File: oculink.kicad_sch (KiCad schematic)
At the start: 9 parts, among them J1 OCuLink_x4_Amphenol_G14A42121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

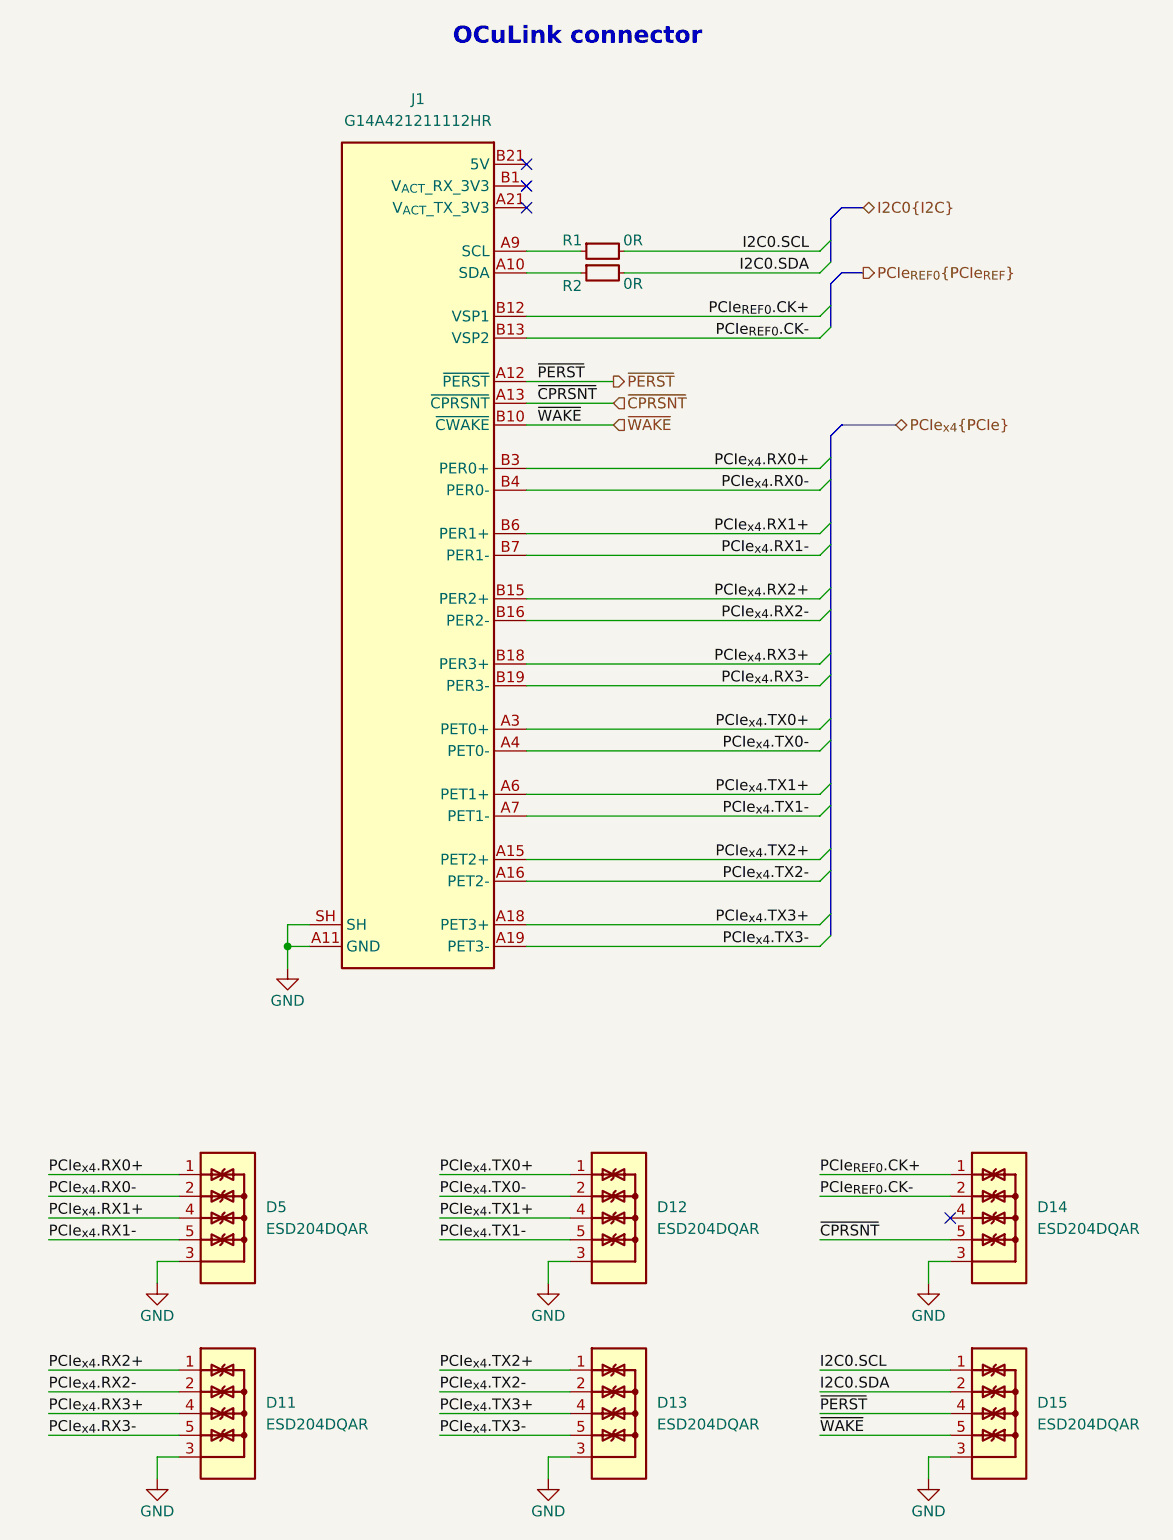
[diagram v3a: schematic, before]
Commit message: [#79426] Add optional clock generator
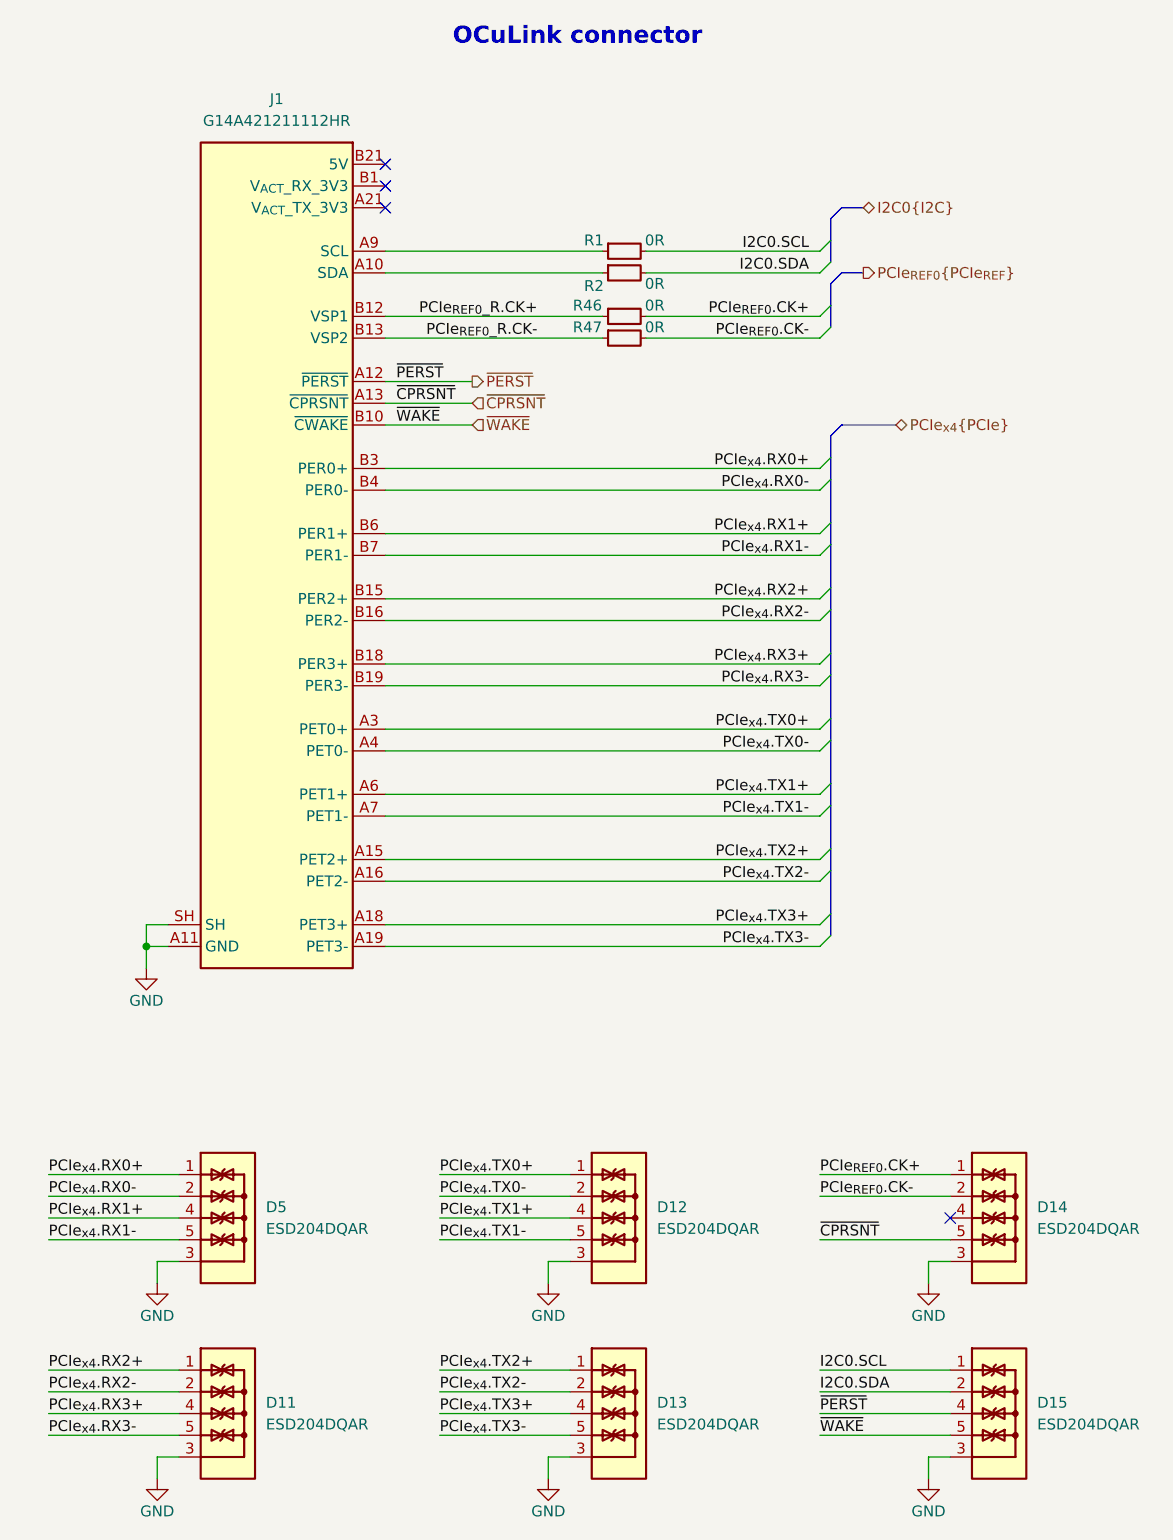
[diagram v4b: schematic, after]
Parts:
- added R46, R47: R_0R_0402, antmicro-footprints:R_0402_1005Metric, symbol antmicroResistors0402:R_0R_0402
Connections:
- net PCIe_{REF0}.CK+: now also R46.2; no longer J1.B12 (VSP1)
- net PCIe_{REF0}.CK-: now also R47.2; no longer J1.B13 (VSP2)
- new net PCIe_{REF0}_R.CK+: J1.B12 (VSP1), R46.1
- new net PCIe_{REF0}_R.CK-: J1.B13 (VSP2), R47.1
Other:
- moved on the sheet: J1, R1, R2

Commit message: [#79426] Add 0R to OCuLink control signals
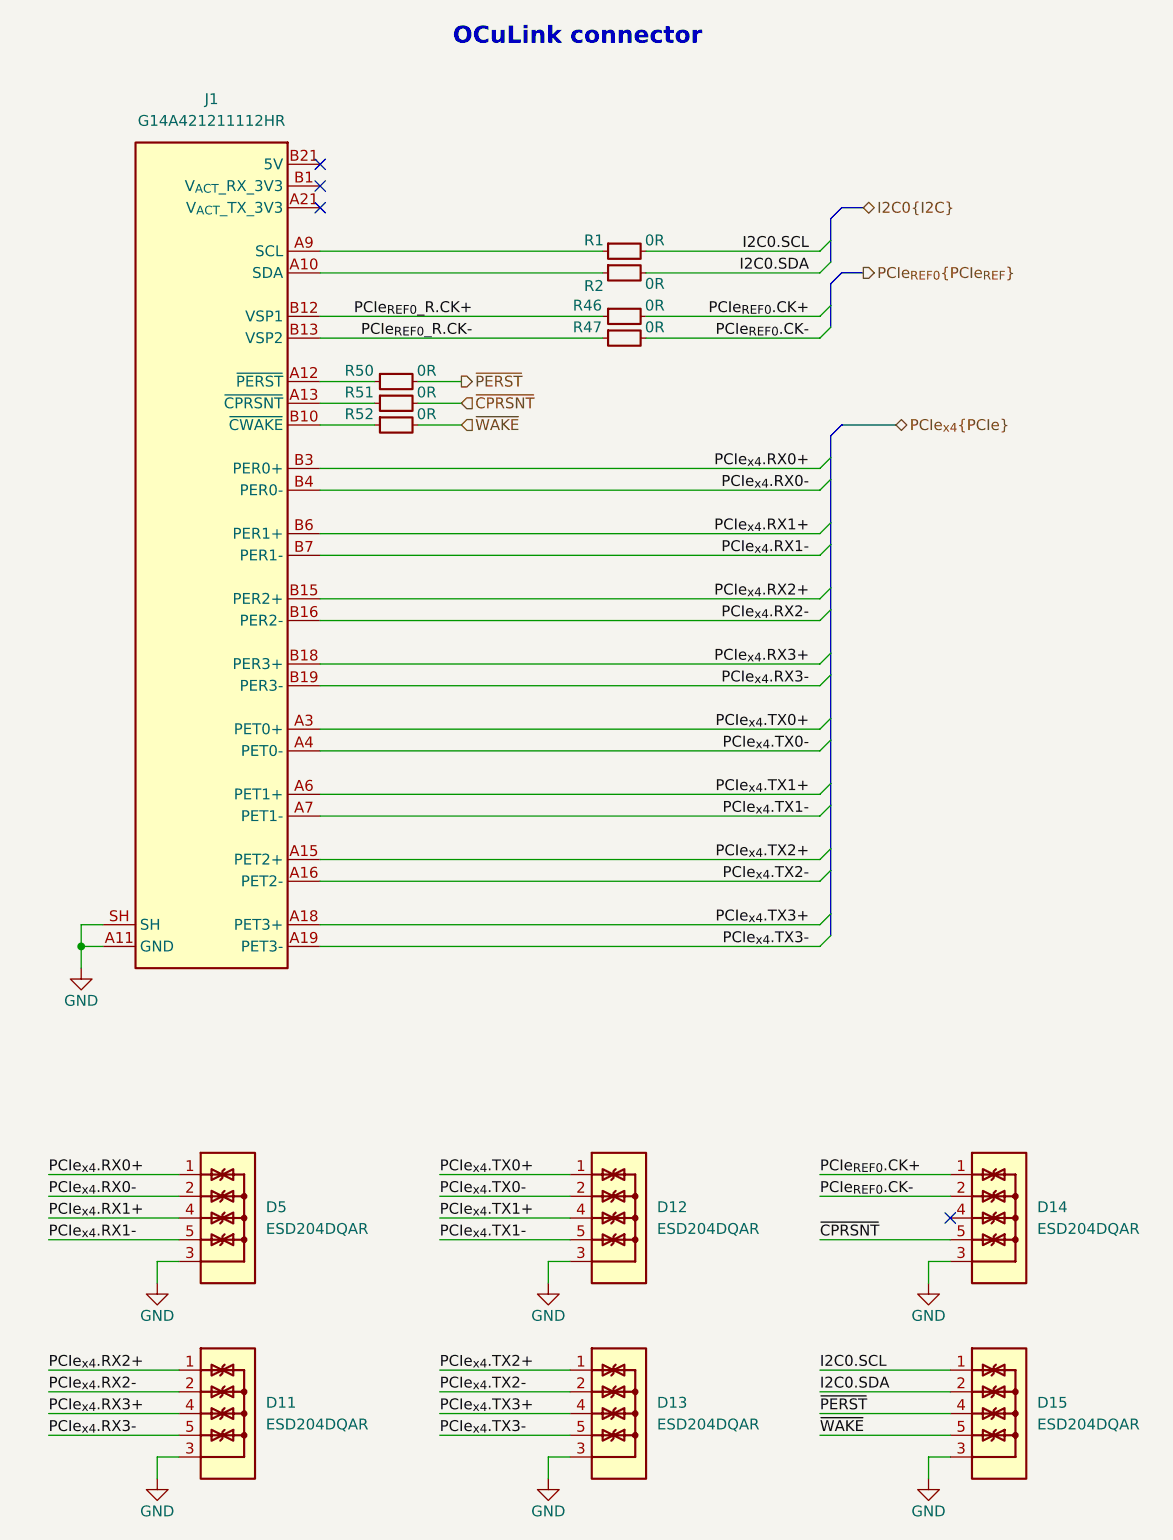
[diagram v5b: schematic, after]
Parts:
- added R50, R51, R52: R_0R_0402, antmicro-footprints:R_0402_1005Metric, symbol antmicroResistors0402:R_0R_0402
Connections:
- net ~{CPRSNT}: now also R51.2; no longer J1.A13 (~{CPRSNT})
- net ~{PERST}: now also R50.2; no longer J1.A12 (~{PERST})
- net ~{WAKE}: now also R52.2; no longer J1.B10 (~{CWAKE})
- new net: J1.B10 (~{CWAKE}), R52.1
- new net: J1.A12 (~{PERST}), R50.1
- new net: J1.A13 (~{CPRSNT}), R51.1
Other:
- moved on the sheet: J1

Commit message: [#79262] WIP: Component placement
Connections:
- net PCIe_{REF0}.CK+: no longer D14.1, D14.10
- net PCIe_{REF0}.CK-: no longer D14.2, D14.9
- net PCIe_{REF0}_R.CK+: now also D14.1, D14.10
- net PCIe_{REF0}_R.CK-: now also D14.2, D14.9
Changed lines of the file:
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@@
-		)
-	)
-	(label "PCIe_{REF0}.CK+"
-		(at 231.14 210.82 0)
-		(effects
-			(font
-				(size 1.27 1.27)
-			)
-			(justify left bottom)
 		)
 	)
@@
 		)
 	)
-	(label "PCIe_{REF0}.CK-"
-		(at 231.14 213.36 0)
-		(effects
-			(font
-				(size 1.27 1.27)
-			)
-			(justify left bottom)
-		)
-	)
 	(label "PCIe_{x4}.TX2-"
 		(at 186.69 236.22 0)
@@
 			)
 			(justify right bottom)
+		)
+	)
+	(label "PCIe_{REF0}_R.CK+"
+		(at 231.14 210.82 0)
+		(effects
+			(font
+				(size 1.27 1.27)
+			)
+			(justify left bottom)
 		)
 	)
@@
 		(effects
 			(font
+				(size 1.27 1.27)
+			)
+			(justify left bottom)
+		)
+	)
+	(label "PCIe_{REF0}_R.CK-"
+		(at 231.14 213.36 0)
+		(effects
+			(font

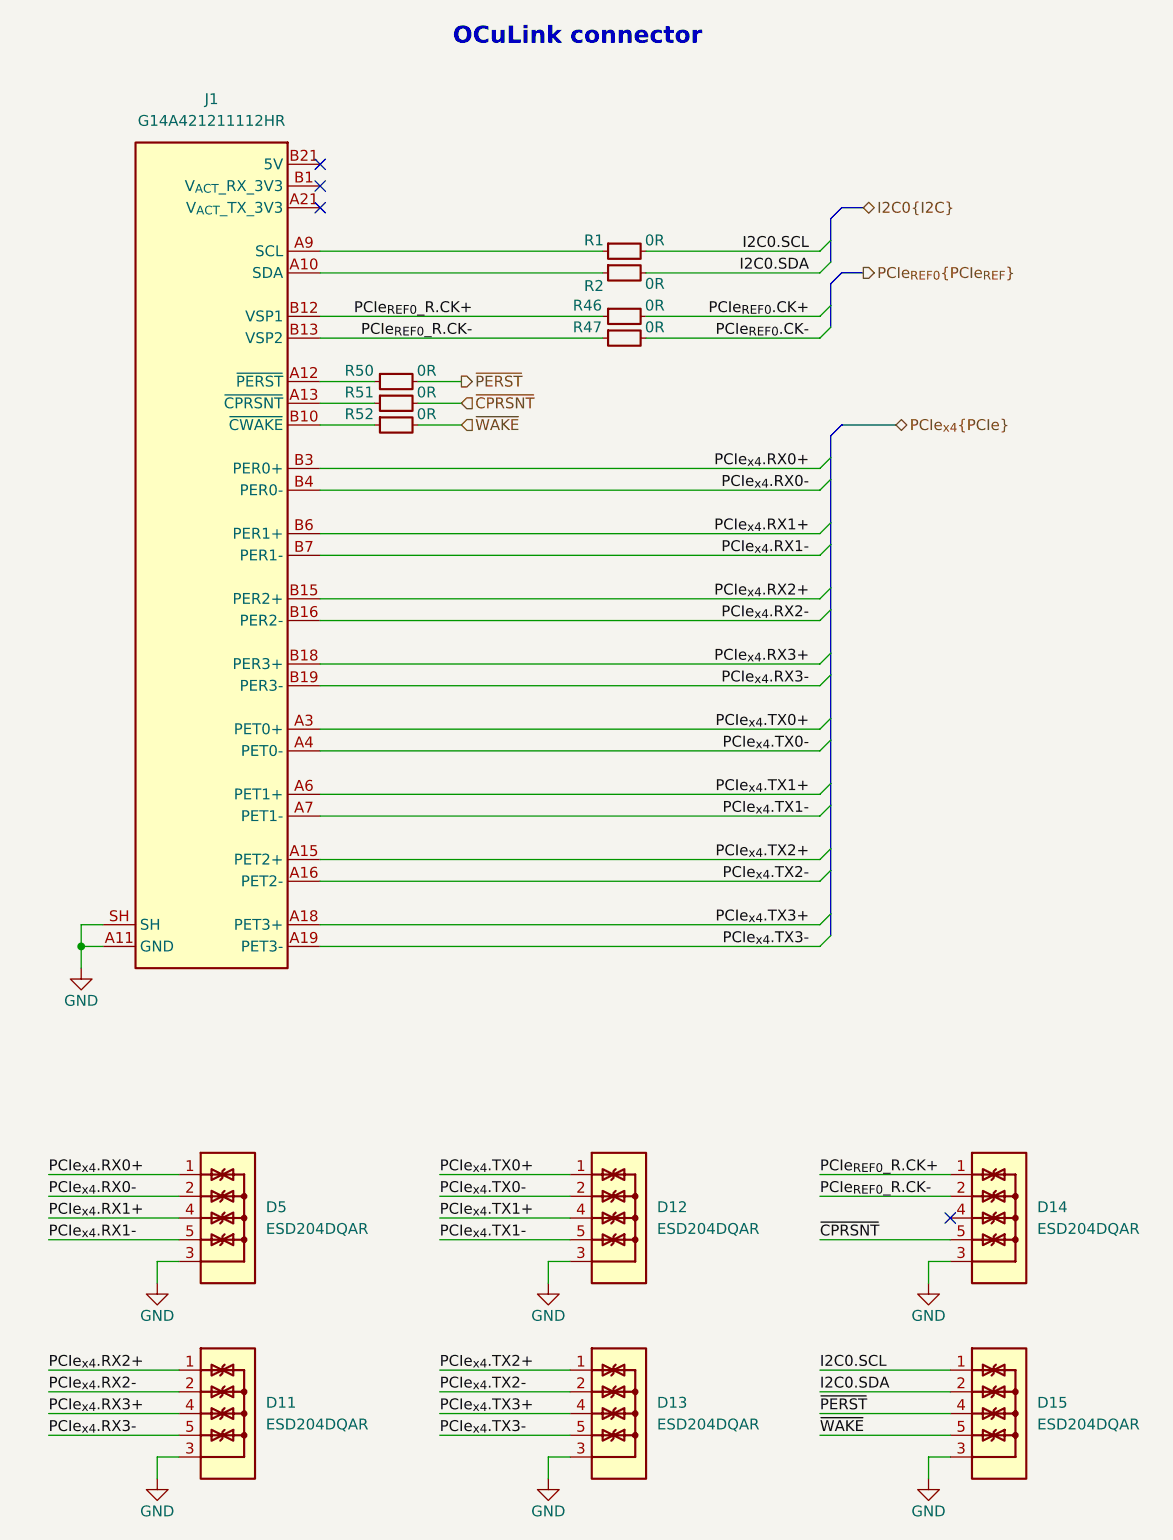
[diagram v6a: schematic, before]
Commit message: [#79262] Adjusted placement
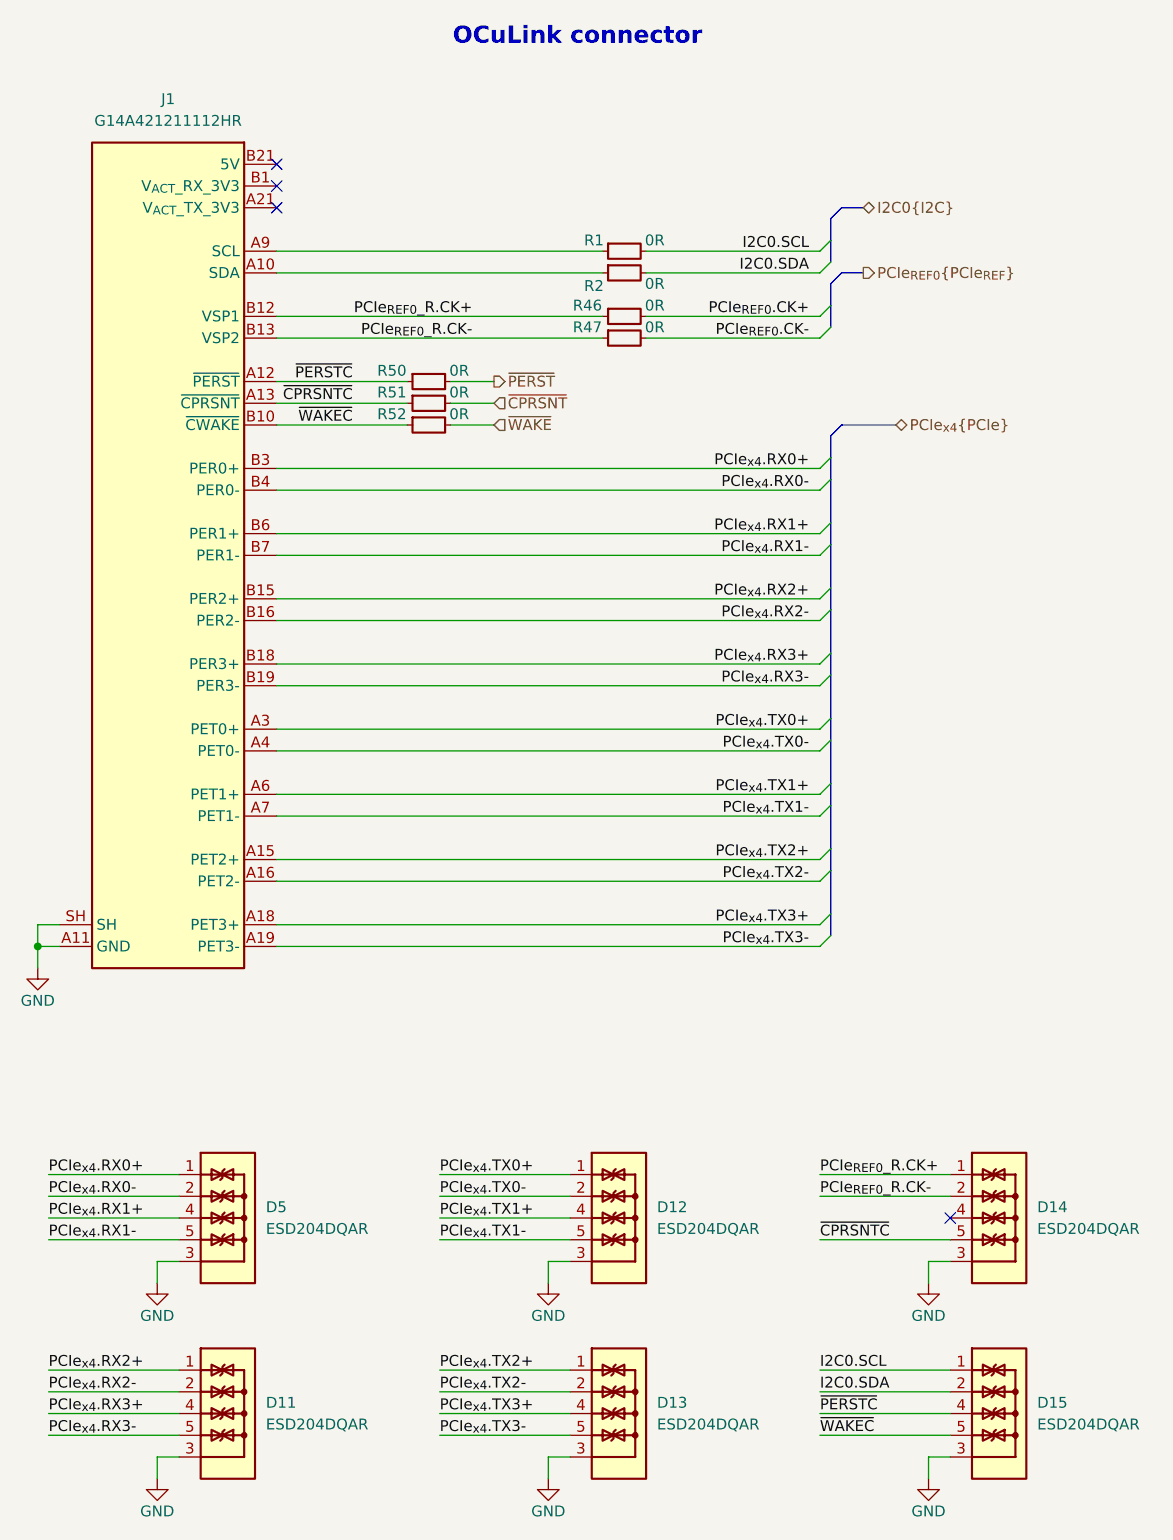
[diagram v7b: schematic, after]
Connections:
- net ~{CPRSNT}: no longer D14.5, D14.6
- net ~{PERST}: no longer D15.4, D15.7
- net ~{WAKE}: no longer D15.5, D15.6
- net ~{WAKEC}: now reaches J1.B10 (~{CWAKE}), R52.1
- net ~{WAKEC}: now also D15.5, D15.6
- net ~{PERSTC}: now reaches J1.A12 (~{PERST}), R50.1
- net ~{PERSTC}: now also D15.4, D15.7
- net ~{CPRSNTC}: now reaches J1.A13 (~{CPRSNT}), R51.1
- net ~{CPRSNTC}: now also D14.5, D14.6
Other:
- moved on the sheet: J1, R50, R51, R52
